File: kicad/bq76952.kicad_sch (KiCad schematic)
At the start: 88 parts, among them Q1 DMN10H220LE, U4 BQ76952

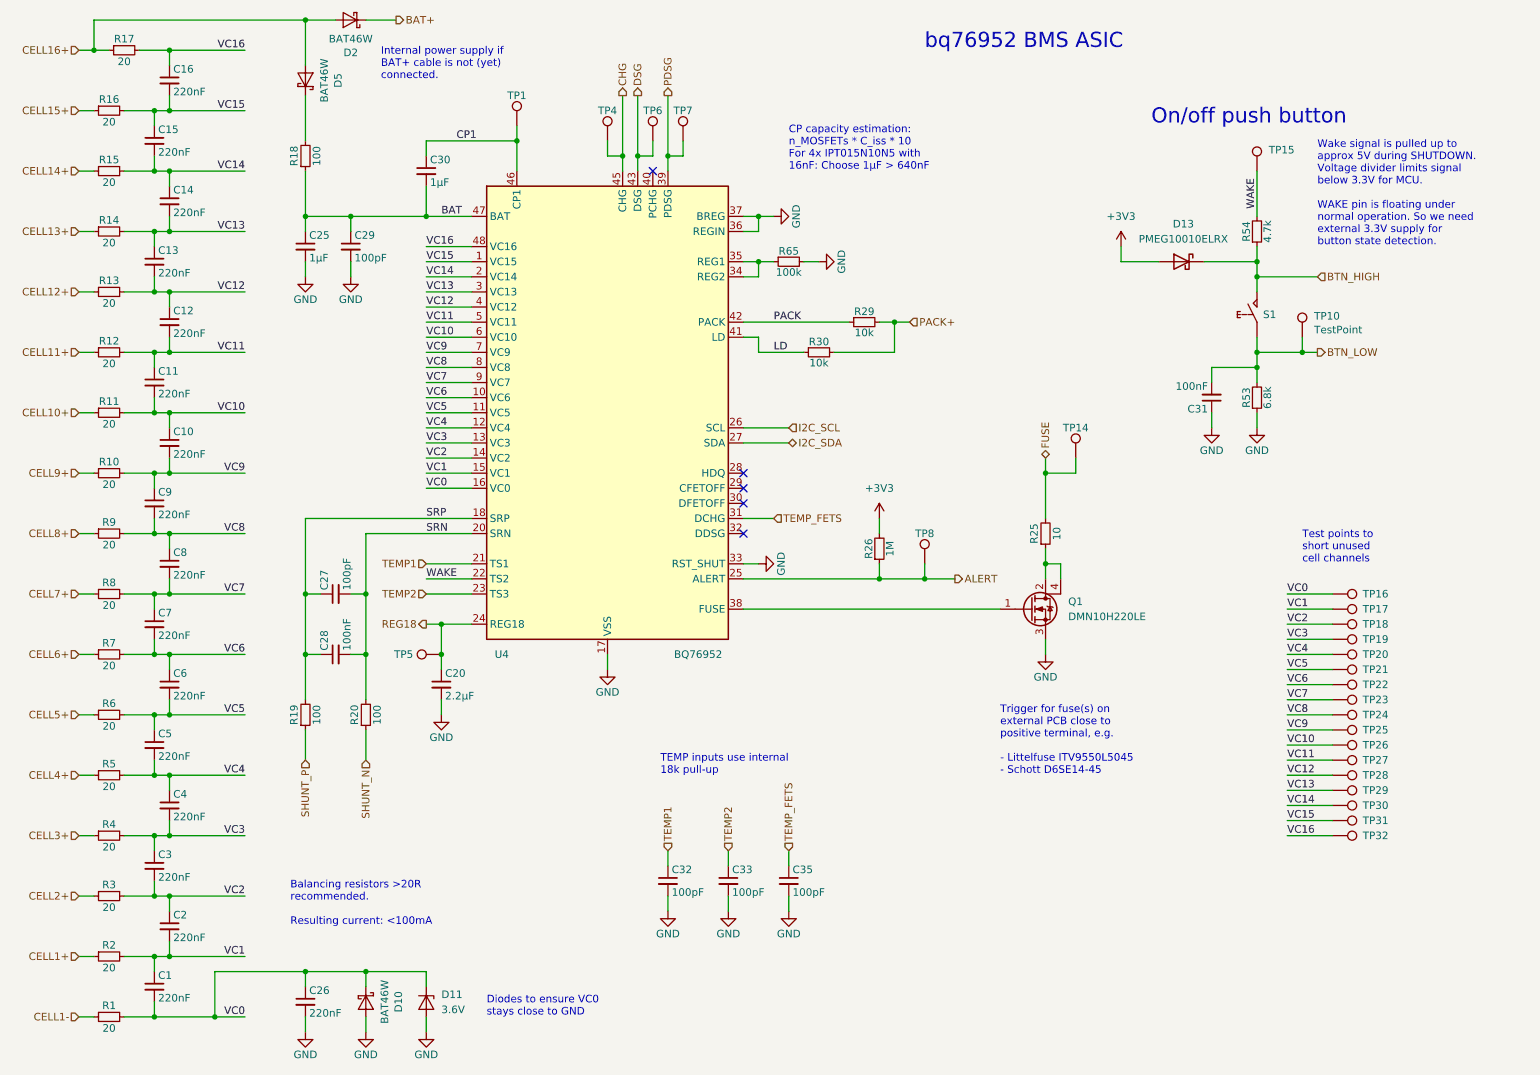
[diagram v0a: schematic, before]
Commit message: v0.4.0: Multiple improvements for new board revision
- Use LMR38010 for internal power supply (max. 80V instead of 60V)
- Change USB connector from Micro-A to C and remove 5V power supply
  which was not working anyway. The board cannot be powered by USB
  only.
- Add TS2 (connected to DFETOFF) to measure shunt temperature
- Add RS-485 transceiver (sharing the connector with CAN)
- Switch I2C pins of ESP32-C3 to GPIO8/9. This allows to re-use the
  I2C pull-ups for strapping configuration and frees two pins for the
  RS-485 transceiver RE and DE pins. Also we may get rid of the I2C
  glitches during start-up.
- Reduce DSG gate resistor R57 to 47R to increase switch-off speed.
- Use more easily available and cheaper Würth 7466005R terminals with
  countersunk hole/thread.
- Adjust some resistors to reduce number of different parts
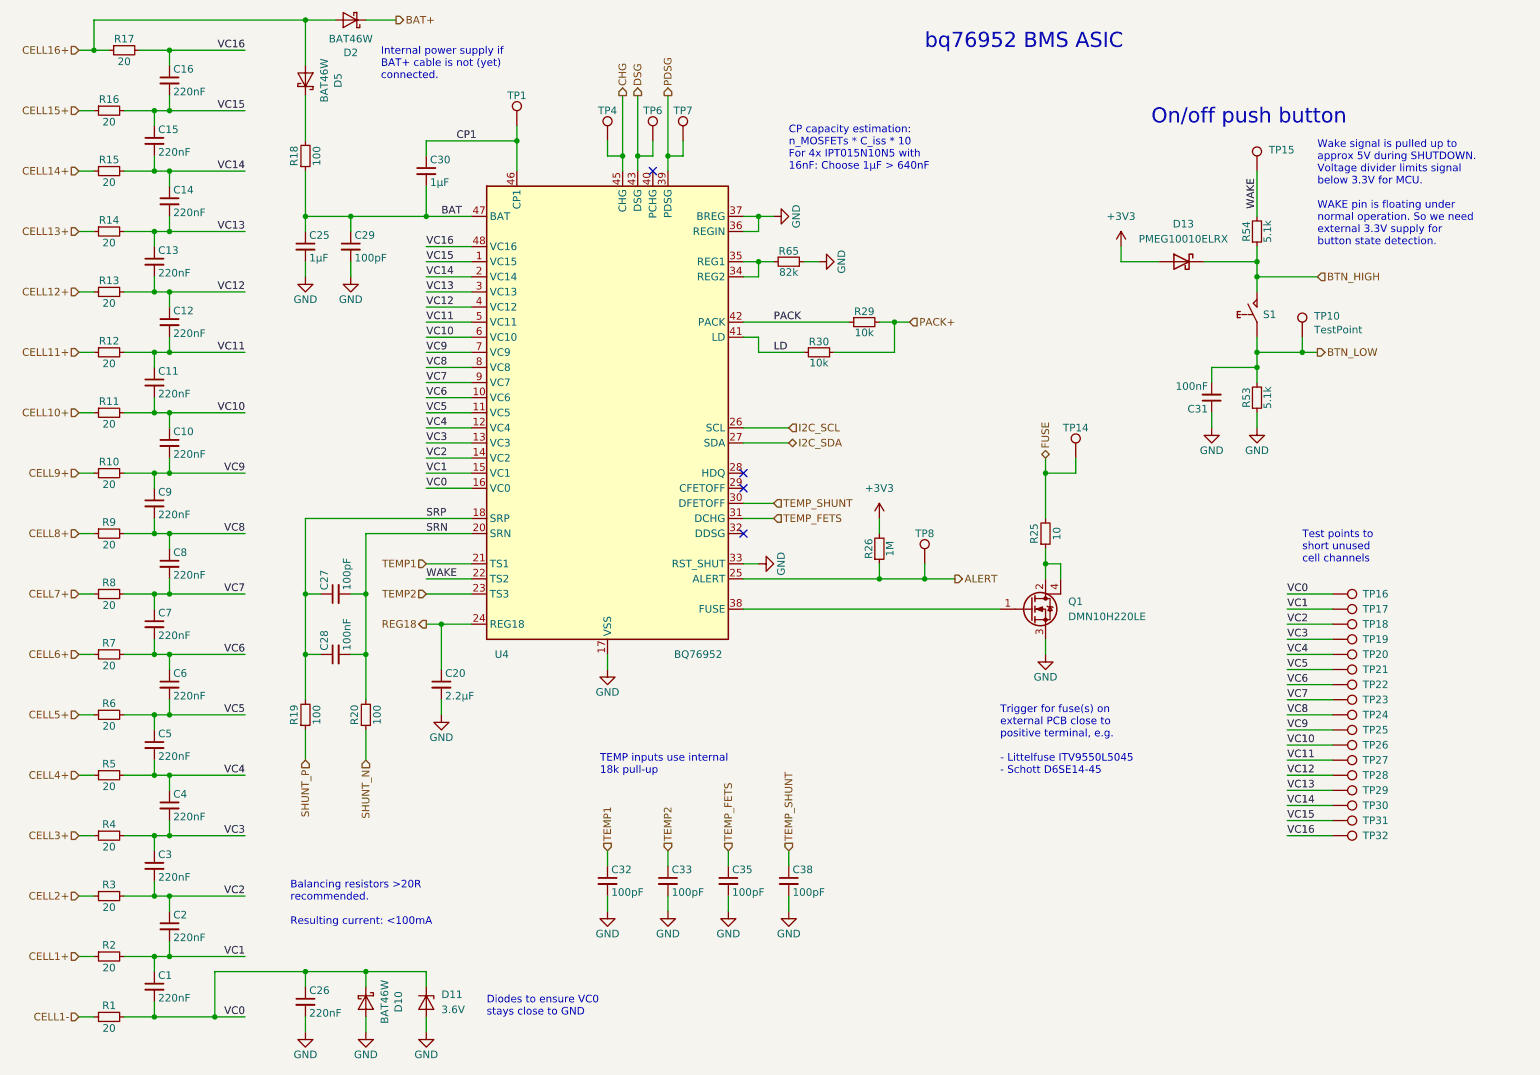
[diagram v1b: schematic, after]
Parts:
- removed TP5: TestPoint, TestPoint:TestPoint_Pad_D1.5mm, symbol Connector:TestPoint
- added C38: 100pF, LibreSolar:C_0603_1608, symbol LibreSolar:C
- R53: value 6.8k -> 5.1k
- R54: value 4.7k -> 5.1k
- R65: value 100k -> 82k
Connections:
- net GND: now also C38.2
- net TEMP_SHUNT: now reaches U4.30 (DFETOFF)
- net TEMP_SHUNT: now also C38.1
- no-connect marks 5 -> 4
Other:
- moved on the sheet: C32, C33, C35
